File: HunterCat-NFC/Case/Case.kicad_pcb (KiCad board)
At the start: 2 copper layers, 80.7 x 33.5 mm, 9 parts

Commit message: update graphic
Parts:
- added Ref**: Val**, Ilustracion Final HC-NFC, B.Cu at (120.3, 92.3)

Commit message: Fixed Case
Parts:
- moved REF** 0.17 mm to (138.3, 82.8)
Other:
- outline, holes or cut-outs redrawn
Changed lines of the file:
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@@
   (general
     (thickness 1.6)
-    (drawings 10)
+    (drawings 14)
     (tracks 0)
     (zones 0)
@@
     (mod_text_size 1 1)
     (mod_text_width 0.15)
-    (pad_size 1.524 1.524)
-    (pad_drill 0.762)
+    (pad_size 3 3)
+    (pad_drill 3)
     (pad_to_mask_clearance 0.05)
     (aux_axis_origin 0 0)
@@
     (uvia_drill 0.1)
   )
+  (module MountingHole:MountingHole_2.2mm_M2 (layer F.Cu)
+    (at 138.3 82.81)
+    (descr "Mounting Hole 2.2mm, no annular, M2")
+    (tags "mounting hole 2.2mm no annular m2")
+    (attr virtual)
+    (fp_text reference REF** (at 0 -3.2) (layer F.Fab)
+      (effects (font (size 1 1) (thickness 0.15)))
+    )
+    (fp_text value MountingHole_2.2mm_M2 (at 0 3.2) (layer F.Fab)
+      (effects (font (size 1 1) (thickness 0.15)))
+    )
+    (fp_text user %R (at 0.3 0) (layer F.Fab)
+      (effects (font (size 1 1) (thickness 0.15)))
+    )
+    (fp_circle (center 0 0) (end 2.45 0) (layer F.CrtYd) (width 0.05))
+    (fp_circle (center 0 0) (end 2.2 0) (layer Cmts.User) (width 0.15))
+    (pad "" np_thru_hole circle (at -0.09 0) (size 3 3) (drill 3) (layers *.Cu *.Mask))
+  )
   (module "Ilustracion Final HC-NFC" (layer B.Cu)
     (at 120.35 92.32 90)
@@
       (effects (font (size 1 1) (thickness 0.15)))
     )
-    (pad 1 np_thru_hole circle (at 0 0) (size 2.2 2.2) (drill 2.2) (layers *.Cu *.Mask))
+    (pad "" np_thru_hole circle (at 0 0) (size 3 3) (drill 3) (layers *.Cu *.Mask))
   )
   (module MountingHole:MountingHole_2.2mm_M2 (layer F.Cu)
@@
       (effects (font (size 1 1) (thickness 0.15)))
     )
-    (pad 1 np_thru_hole circle (at 0 0) (size 2.2 2.2) (drill 2.2) (layers *.Cu *.Mask))
-  )
-  (module MountingHole:MountingHole_2.2mm_M2 (layer F.Cu)
-    (at 138.17 82.7)
-    (descr "Mounting Hole 2.2mm, no annular, M2")
-    (tags "mounting hole 2.2mm no annular m2")
-    (attr virtual)
-    (fp_text reference REF** (at 0 -3.2) (layer F.Fab)
-      (effects (font (size 1 1) (thickness 0.15)))
-    )
-    (fp_text value MountingHole_2.2mm_M2 (at 0 3.2) (layer F.Fab)
-      (effects (font (size 1 1) (thickness 0.15)))
-    )
-    (fp_circle (center 0 0) (end 2.2 0) (layer Cmts.User) (width 0.15))
-    (fp_circle (center 0 0) (end 2.45 0) (layer F.CrtYd) (width 0.05))
-    (fp_text user %R (at 0.3 0) (layer F.Fab)
-      (effects (font (size 1 1) (thickness 0.15)))
-    )
-    (pad 1 np_thru_hole circle (at 0 0) (size 2.2 2.2) (drill 2.2) (layers *.Cu *.Mask))
+    (pad "" np_thru_hole circle (at 0 0) (size 3 3) (drill 3) (layers *.Cu *.Mask))
   )
   (module MountingHole:MountingHole_2.2mm_M2 (layer F.Cu)
@@
       (effects (font (size 1 1) (thickness 0.15)))
     )
-    (pad 1 np_thru_hole circle (at 0 0) (size 2.2 2.2) (drill 2.2) (layers *.Cu *.Mask))
+    (pad "" np_thru_hole circle (at 0 0) (size 3 3) (drill 3) (layers *.Cu *.Mask))
   )
   (module MountingHole:MountingHole_2.2mm_M2 (layer F.Cu)
@@
     (pad 1 np_thru_hole circle (at 0 0) (size 2.2 2.2) (drill 2.2) (layers *.Cu *.Mask))
   )
+  (gr_line (start 107.4 96) (end 107.4 104.5) (layer Edge.Cuts) (width 0.05))
+  (gr_line (start 111.45 96) (end 107.4 96) (layer Edge.Cuts) (width 0.05))
+  (gr_line (start 111.45 104.5) (end 111.45 96) (layer Edge.Cuts) (width 0.05))
+  (gr_line (start 107.4 104.5) (end 111.45 104.5) (layer Edge.Cuts) (width 0.05))
   (dimension 80.690001 (width 0.15) (layer Margin)
     (gr_text "80.690 mm" (at 120.340279 67.904183) (layer Margin)

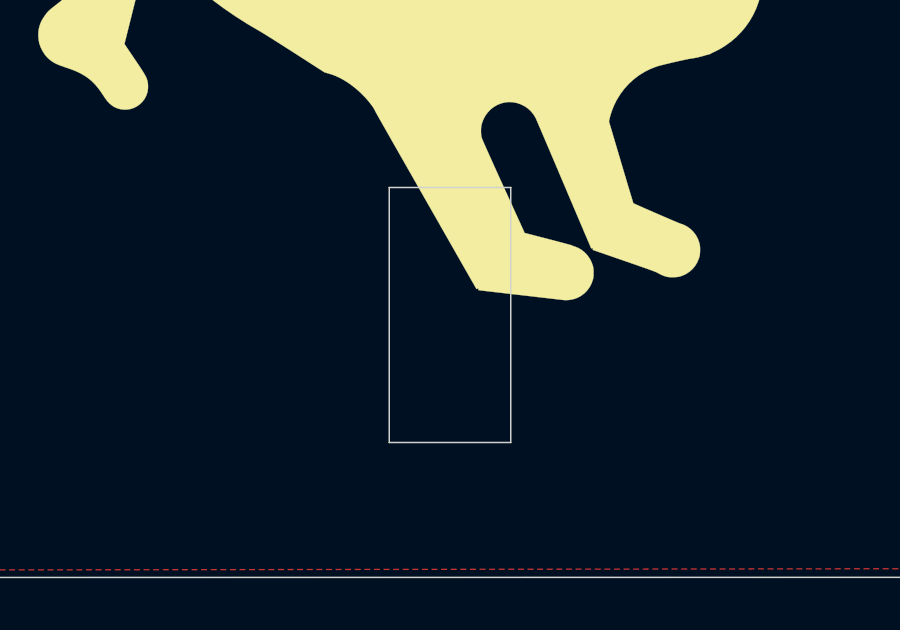
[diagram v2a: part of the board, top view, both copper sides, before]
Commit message: Fixed Led window
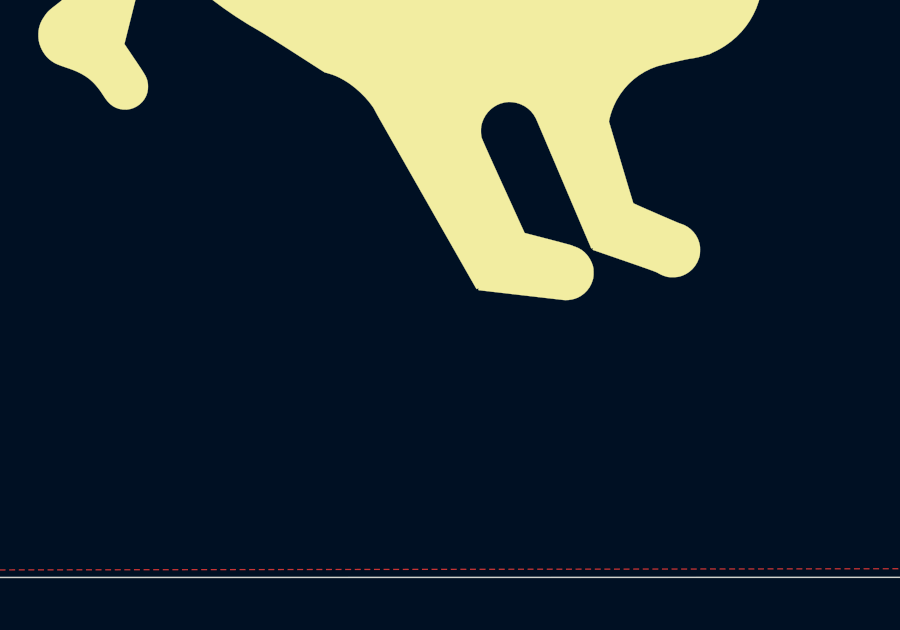
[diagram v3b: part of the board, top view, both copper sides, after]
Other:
- outline, holes or cut-outs redrawn
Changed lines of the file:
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@@
   (general
     (thickness 1.6)
-    (drawings 14)
+    (drawings 26)
     (tracks 0)
     (zones 0)
@@
     (47 F.CrtYd user)
     (48 B.Fab user hide)
-    (49 F.Fab user hide)
+    (49 F.Fab user)
   )
   (setup
@@
     (pad 1 np_thru_hole circle (at 0 0) (size 2.2 2.2) (drill 2.2) (layers *.Cu *.Mask))
   )
-  (gr_line (start 107.4 96) (end 107.4 104.5) (layer Edge.Cuts) (width 0.05))
-  (gr_line (start 111.45 96) (end 107.4 96) (layer Edge.Cuts) (width 0.05))
-  (gr_line (start 111.45 104.5) (end 111.45 96) (layer Edge.Cuts) (width 0.05))
-  (gr_line (start 107.4 104.5) (end 111.45 104.5) (layer Edge.Cuts) (width 0.05))
+  (gr_line (start 111.46 80) (end 107.41 80) (layer F.Fab) (width 0.15))
+  (gr_line (start 111.46 88.51) (end 111.46 80) (layer F.Fab) (width 0.15))
+  (gr_line (start 107.4 88.51) (end 111.46 88.51) (layer F.Fab) (width 0.15))
+  (gr_line (start 107.4 80) (end 107.4 88.51) (layer F.Fab) (width 0.15))
+  (dimension 5.85 (width 0.05) (layer F.CrtYd)
+    (gr_text "5.850 mm" (at 110.325 76.6) (layer F.CrtYd)
+      (effects (font (size 1 1) (thickness 0.15)))
+    )
+    (feature1 (pts (xy 113.25 80) (xy 113.25 77.213579)))
+    (feature2 (pts (xy 107.4 80) (xy 107.4 77.213579)))
+    (crossbar (pts (xy 107.4 77.8) (xy 113.25 77.8)))
+    (arrow1a (pts (xy 113.25 77.8) (xy 112.123496 78.386421)))
+    (arrow1b (pts (xy 113.25 77.8) (xy 112.123496 77.213579)))
+    (arrow2a (pts (xy 107.4 77.8) (xy 108.526504 78.386421)))
+    (arrow2b (pts (xy 107.4 77.8) (xy 108.526504 77.213579)))
+  )
+  (dimension 4.06 (width 0.05) (layer F.CrtYd)
+    (gr_text "4.060 mm" (at 109.43 91.41) (layer F.CrtYd)
+      (effects (font (size 1 1) (thickness 0.15)))
+    )
+    (feature1 (pts (xy 111.46 88.51) (xy 111.46 90.796421)))
+    (feature2 (pts (xy 107.4 88.51) (xy 107.4 90.796421)))
+    (crossbar (pts (xy 107.4 90.21) (xy 111.46 90.21)))
+    (arrow1a (pts (xy 111.46 90.21) (xy 110.333496 90.796421)))
+    (arrow1b (pts (xy 111.46 90.21) (xy 110.333496 89.623579)))
+    (arrow2a (pts (xy 107.4 90.21) (xy 108.526504 90.796421)))
+    (arrow2b (pts (xy 107.4 90.21) (xy 108.526504 89.623579)))
+  )
+  (dimension 4.05 (width 0.05) (layer F.CrtYd)
+    (gr_text "4.050 mm" (at 109.425 93.47) (layer F.CrtYd)
+      (effects (font (size 1 1) (thickness 0.15)))
+    )
+    (feature1 (pts (xy 111.45 96) (xy 111.45 94.083579)))
+    (feature2 (pts (xy 107.4 96) (xy 107.4 94.083579)))
+    (crossbar (pts (xy 107.4 94.67) (xy 111.45 94.67)))
+    (arrow1a (pts (xy 111.45 94.67) (xy 110.323496 95.256421)))
+    (arrow1b (pts (xy 111.45 94.67) (xy 110.323496 94.083579)))
+    (arrow2a (pts (xy 107.4 94.67) (xy 108.526504 95.256421)))
+    (arrow2b (pts (xy 107.4 94.67) (xy 108.526504 94.083579)))
+  )
+  (dimension 8.51 (width 0.05) (layer F.CrtYd)
+    (gr_text "8.510 mm" (at 97.49 84.255 270) (layer F.CrtYd)
+      (effects (font (size 1 1) (thickness 0.15)))
+    )
+    (feature1 (pts (xy 107.4 88.51) (xy 98.103579 88.51)))
+    (feature2 (pts (xy 107.4 80) (xy 98.103579 80)))
+    (crossbar (pts (xy 98.69 80) (xy 98.69 88.51)))
+    (arrow1a (pts (xy 98.69 88.51) (xy 98.103579 87.383496)))
+    (arrow1b (pts (xy 98.69 88.51) (xy 99.276421 87.383496)))
+    (arrow2a (pts (xy 98.69 80) (xy 98.103579 81.126504)))
+    (arrow2b (pts (xy 98.69 80) (xy 99.276421 81.126504)))
+  )
+  (dimension 8.49 (width 0.05) (layer F.CrtYd)
+    (gr_text "8.490 mm" (at 104.26 100.245 90) (layer F.CrtYd)
+      (effects (font (size 1 1) (thickness 0.15)))
+    )
+    (feature1 (pts (xy 107.4 96) (xy 104.873579 96)))
+    (feature2 (pts (xy 107.4 104.49) (xy 104.873579 104.49)))
+    (crossbar (pts (xy 105.46 104.49) (xy 105.46 96)))
+    (arrow1a (pts (xy 105.46 96) (xy 106.046421 97.126504)))
+    (arrow1b (pts (xy 105.46 96) (xy 104.873579 97.126504)))
+    (arrow2a (pts (xy 105.46 104.49) (xy 106.046421 103.363496)))
+    (arrow2b (pts (xy 105.46 104.49) (xy 104.873579 103.363496)))
+  )
+  (dimension 4.5 (width 0.05) (layer F.CrtYd)
+    (gr_text "4.500 mm" (at 105.11 77.75 270) (layer F.CrtYd)
+      (effects (font (size 1 1) (thickness 0.15)))
+    )
+    (feature1 (pts (xy 107.4 80) (xy 105.723579 80)))
+    (feature2 (pts (xy 107.4 75.5) (xy 105.723579 75.5)))
+    (crossbar (pts (xy 106.31 75.5) (xy 106.31 80)))
+    (arrow1a (pts (xy 106.31 80) (xy 105.723579 78.873496)))
+    (arrow1b (pts (xy 106.31 80) (xy 106.896421 78.873496)))
+    (arrow2a (pts (xy 106.31 75.5) (xy 105.723579 76.626504)))
+    (arrow2b (pts (xy 106.31 75.5) (xy 106.896421 76.626504)))
+  )
+  (dimension 4.51 (width 0.05) (layer F.CrtYd)
+    (gr_text "4.510 mm" (at 100.28 106.745 270) (layer F.CrtYd)
+      (effects (font (size 1 1) (thickness 0.15)))
+    )
+    (feature1 (pts (xy 107.4 109) (xy 100.893579 109)))
+    (feature2 (pts (xy 107.4 104.49) (xy 100.893579 104.49)))
+    (crossbar (pts (xy 101.48 104.49) (xy 101.48 109)))
+    (arrow1a (pts (xy 101.48 109) (xy 100.893579 107.873496)))
+    (arrow1b (pts (xy 101.48 109) (xy 102.066421 107.873496)))
+    (arrow2a (pts (xy 101.48 104.49) (xy 100.893579 105.616504)))
+    (arrow2b (pts (xy 101.48 104.49) (xy 102.066421 105.616504)))
+  )
+  (dimension 20.5 (width 0.05) (layer F.CrtYd)
+    (gr_text "20.500 mm" (at 101.73 85.75 90) (layer F.CrtYd)
+      (effects (font (size 1 1) (thickness 0.15)))
+    )
+    (feature1 (pts (xy 107.4 75.5) (xy 102.343579 75.5)))
+    (feature2 (pts (xy 107.4 96) (xy 102.343579 96)))
+    (crossbar (pts (xy 102.93 96) (xy 102.93 75.5)))
+    (arrow1a (pts (xy 102.93 75.5) (xy 103.516421 76.626504)))
+    (arrow1b (pts (xy 102.93 75.5) (xy 102.343579 76.626504)))
+    (arrow2a (pts (xy 102.93 96) (xy 103.516421 94.873496)))
+    (arrow2b (pts (xy 102.93 96) (xy 102.343579 94.873496)))
+  )
+  (gr_line (start 107.4 96) (end 107.4 104.5) (layer F.Fab) (width 0.05))
+  (gr_line (start 111.45 96) (end 107.4 96) (layer F.Fab) (width 0.05))
+  (gr_line (start 111.45 104.5) (end 111.45 96) (layer F.Fab) (width 0.05))
+  (gr_line (start 107.4 104.5) (end 111.45 104.5) (layer F.Fab) (width 0.05))
   (dimension 80.690001 (width 0.15) (layer Margin)
     (gr_text "80.690 mm" (at 120.340279 67.904183) (layer Margin)
@@
       )
     )
+  )
+  (zone (net 0) (net_name "") (layers F&B.Cu) (hatch edge 0.508)
+    (connect_pads (clearance 0.508))
+    (min_thickness 0.254)
+    (keepout (tracks not_allowed) (vias not_allowed) (copperpour not_allowed))
+    (fill (arc_segments 32) (thermal_gap 0.508) (thermal_bridge_width 0.508))
+    (polygon
+      (pts
+        (xy 111.44 104.49) (xy 107.4 104.49) (xy 107.4 96) (xy 111.44 96)
+      )
+    )
+  )
+  (zone (net 0) (net_name "") (layers F&B.Cu) (hatch edge 0.508)
+    (connect_pads (clearance 0.508))
+    (min_thickness 0.254)
+    (keepout (tracks not_allowed) (vias not_allowed) (copperpour not_allowed))
+    (fill (arc_segments 32) (thermal_gap 0.508) (thermal_bridge_width 0.508))
+    (polygon
+      (pts
+        (xy 111.47 88.51) (xy 107.41 88.51) (xy 107.41 80.01) (xy 111.47 80.01)
+      )
+    )
